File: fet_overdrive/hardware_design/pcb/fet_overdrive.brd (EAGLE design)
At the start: 30 x 107.3 mm, 40 parts, among them IC1 TL072CD, J1 PJ301_THONKICONN6, J2 PJ301_THONKICONN6, Q1 MMBFJ111, Q2 SMMBT3904LT1G

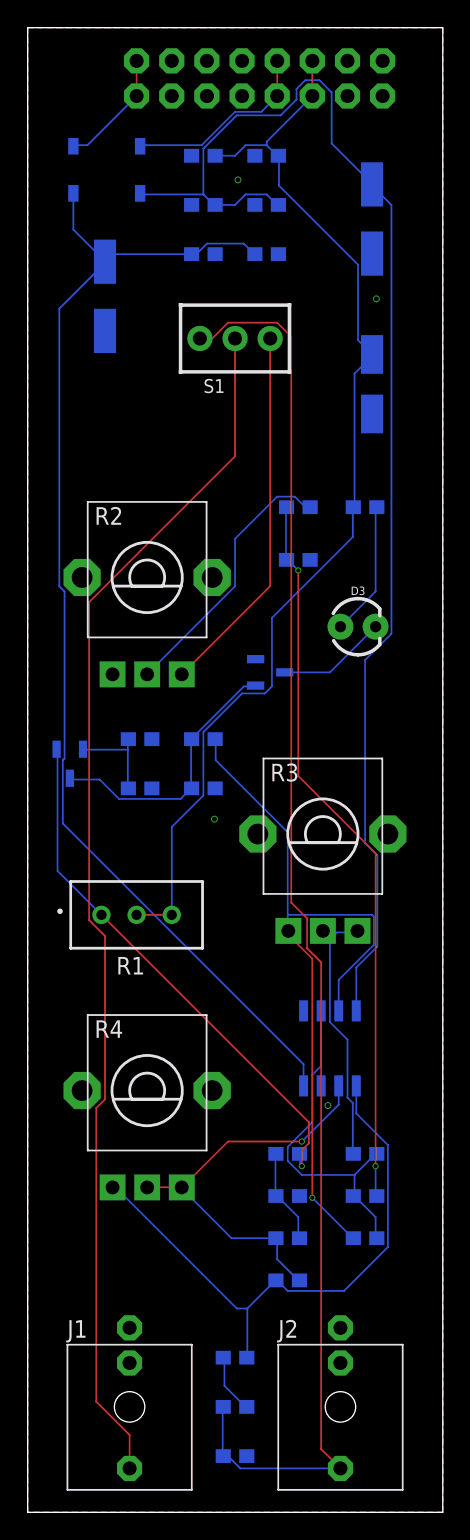
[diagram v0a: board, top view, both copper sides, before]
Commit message: design for fet overdrive and quantizer 2 code updates
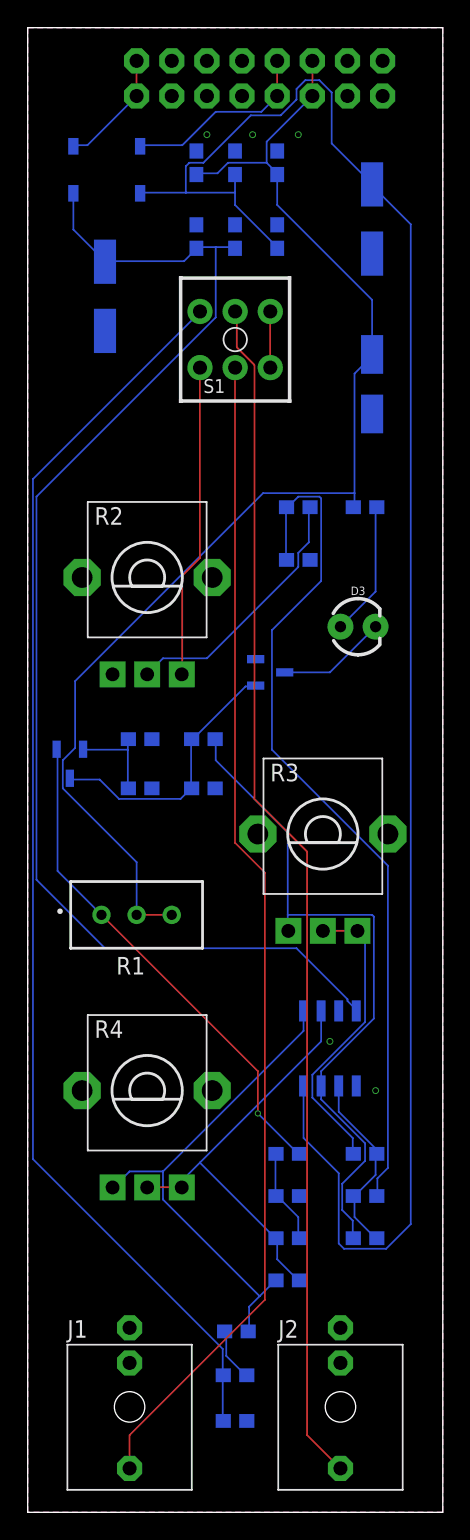
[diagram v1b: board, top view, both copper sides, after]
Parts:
- U$1: device Graphics v21:DAILYWELL -> Graphics v37:DAILYWELL-DPDT
- moved U$1 4.76 mm to (15.0, 84.8)
- moved C8 3.81 mm to (15.0, 97.5), turned to 90 degrees
- moved C9 2.62 mm to (15.0, 92.2), turned to 270 degrees
- moved R14 2.54 mm to (15.0, 6.60)
- moved C7 2.41 mm to (18.0, 92.2), turned to 90 degrees
- moved C16 2.29 mm to (15.0, 9.91)
- moved R13 1.90 mm to (15.1, 13.1)
- moved C10 1.37 mm to (12.2, 92.2), turned to 270 degrees
- moved C5 0.92 mm to (18.0, 97.5), turned to 90 degrees
- moved C6 0.72 mm to (12.2, 97.5), turned to 90 degrees
- turned IC1 to 270 degrees
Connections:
- new net N$1: C16.2, R14.2, U$1.P$4
- new net N$17: J2.P3, U$1.P$5
- net N$15: now also U$1.P$3, U$1.P$6; no longer C16.2, J2.P3, R14.2, U$1.P$1
- net N$6: now also U$1.P$1; no longer U$1.P$3
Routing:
- net N$15: track 103.2 -> 4.06 mm
- net N$1: track 0.00 -> 90.9 mm
- net N$17: track 0.00 -> 86.8 mm
- net VCC: track 96.4 -> 132.0 mm
- net 2IN-: track 24.7 -> 13.6 mm
- net 5V: track 79.9 -> 90.7 mm
- net N$9: track 52.7 -> 62.5 mm, vias 2 -> 0
- net VEE: track 85.9 -> 94.1 mm
- net 1OUT: track 42.2 -> 36.4 mm
- net 2OUT: track 54.4 -> 49.5 mm, vias 1 -> 0
- net N$6: track 26.9 -> 22.7 mm
- net N$2: track 87.8 -> 84.5 mm
- net N$5: track 38.9 -> 36.6 mm
- net N$14: track 20.1 -> 21.7 mm
- net 1IN-: track 29.9 -> 31.1 mm, vias 1 -> 0
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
